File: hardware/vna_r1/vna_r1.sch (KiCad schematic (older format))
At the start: 0 parts

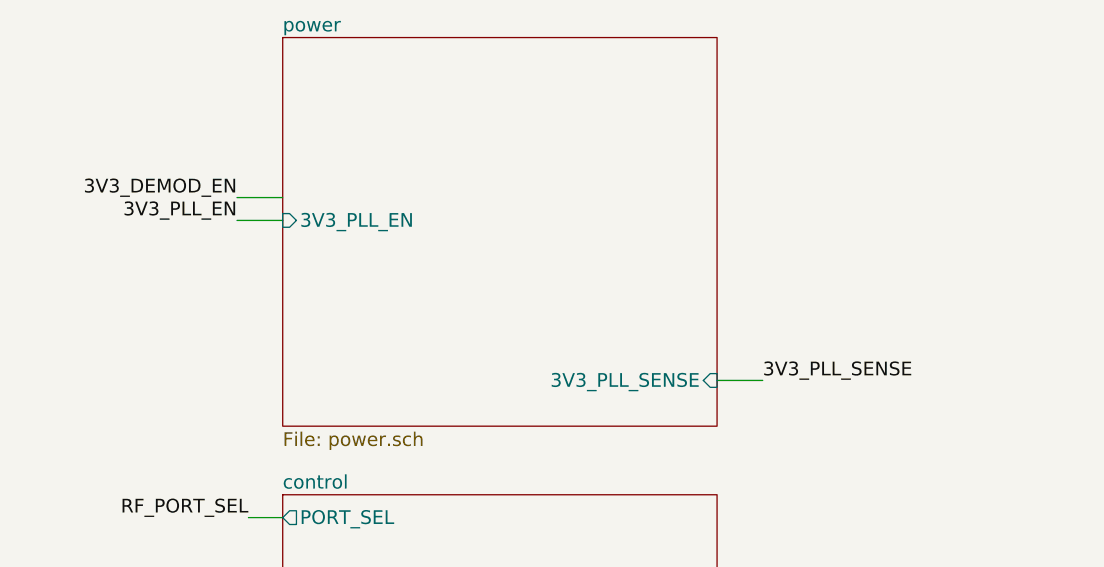
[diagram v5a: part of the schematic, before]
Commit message: component placement on vna r1 demod
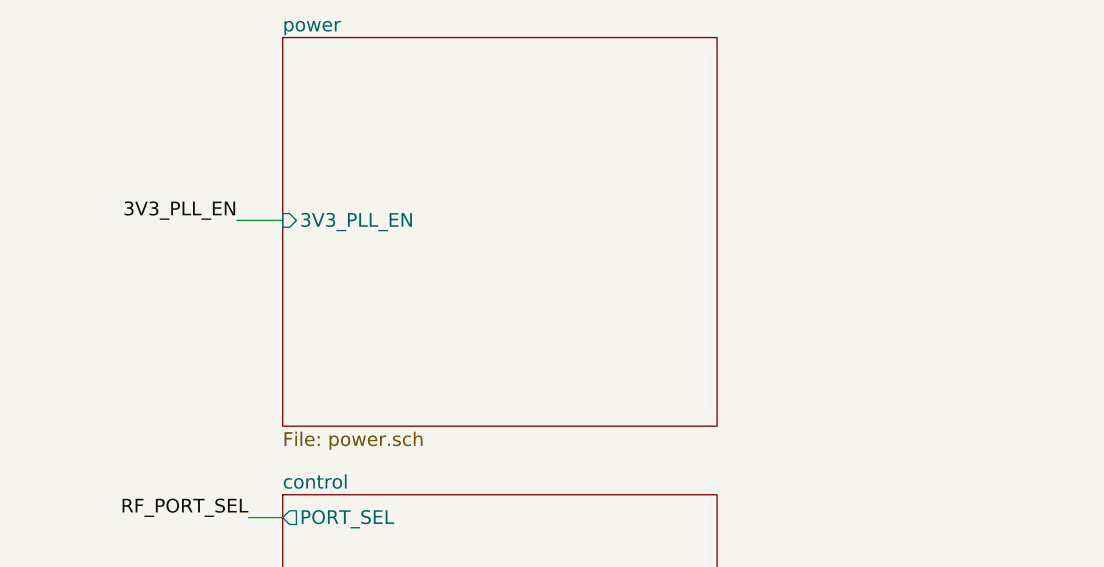
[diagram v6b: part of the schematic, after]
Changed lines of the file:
@@
 F0 "power" 60
 F1 "power.sch" 60
-F4 "3V3_PLL_EN" I L 1650 1900 60
-F5 "3V3_PLL_SENSE" I R 3550 2600 60
+F2 "3V3_PLL_EN" I L 1650 1900 60
 $EndSheet
 Text Label 14350 8350 0    60   ~ 0
@@
 Text Label 14350 7100 0    60   ~ 0
 RF_FILT_SW_2
-Text Label 3750 2600 0    60   ~ 0
-3V3_PLL_SENSE
 Text Label 14350 5650 0    60   ~ 0
 RF_-5V_EN
@@
 Text Label 14350 5950 0    60   ~ 0
 RF_3V3_EN
-Text Label 1450 1800 2    60   ~ 0
-3V3_DEMOD_EN
 Text Label 1450 1900 2    60   ~ 0
 3V3_PLL_EN
@@
 EXT_SPI_CLK
 Wire Wire Line
-	1450 1800 1650 1800
-Wire Wire Line
 	1450 1900 1650 1900
 Wire Wire Line
-	3550 2600 3750 2600
-Wire Wire Line
 	11150 9700 12500 9700

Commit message: layout on r1
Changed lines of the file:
@@
 EXT_UART_MRX
 Text Label 3750 9950 0    60   ~ 0
-EXT_UART_MRX
+EXT_UART_MTX
 Wire Wire Line
 	3550 9850 3750 9850
@@
 EXT_UART_MRX
 Text Label 14900 1700 2    60   ~ 0
-EXT_UART_MRX
+EXT_UART_MTX
 Wire Wire Line
 	14900 1600 15050 1600

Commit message: layout of control board io connector traces
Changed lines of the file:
@@
 F58 "LO_DAC_CS" I L 1650 9150 60
 F59 "ADC_CLK_EN" O L 1650 5850 60
+F60 "LO_BUF_AMP_EN" O L 1650 8300 60
 $EndSheet
 Text Label 14900 1900 2    60   ~ 0
@@
 F33 "LO_SYNTH_CLK" I R 14150 7800 60
 F34 "RF_SYNTH_CLK" I R 14150 6550 60
+F35 "LO_BUF_AMP_EN" I R 14150 9350 60
 $EndSheet
 Wire Wire Line
@@
 Wire Wire Line
 	1650 5850 1500 5850
+Text Label 14350 9350 0    60   ~ 0
+LO_BUF_AMP_EN
+Wire Wire Line
+	14350 9350 14150 9350
+Text Label 1500 8300 2    60   ~ 0
+LO_BUF_AMP_EN
+Wire Wire Line
+	1650 8300 1500 8300
 $EndSCHEMATC
